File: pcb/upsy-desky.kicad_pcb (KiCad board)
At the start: 2 copper layers, 40.9 x 58 mm, 48 parts, among them J1 RJ45, J2 RJ45, J3 USB_C_ReceptacleUSB2.0, Q1 MMBT3904, Q2 MMBT3904, Q3 BSS138, Q4 BSS138, Q5 BSS138, Q6 BSS138, Q7 BSS138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

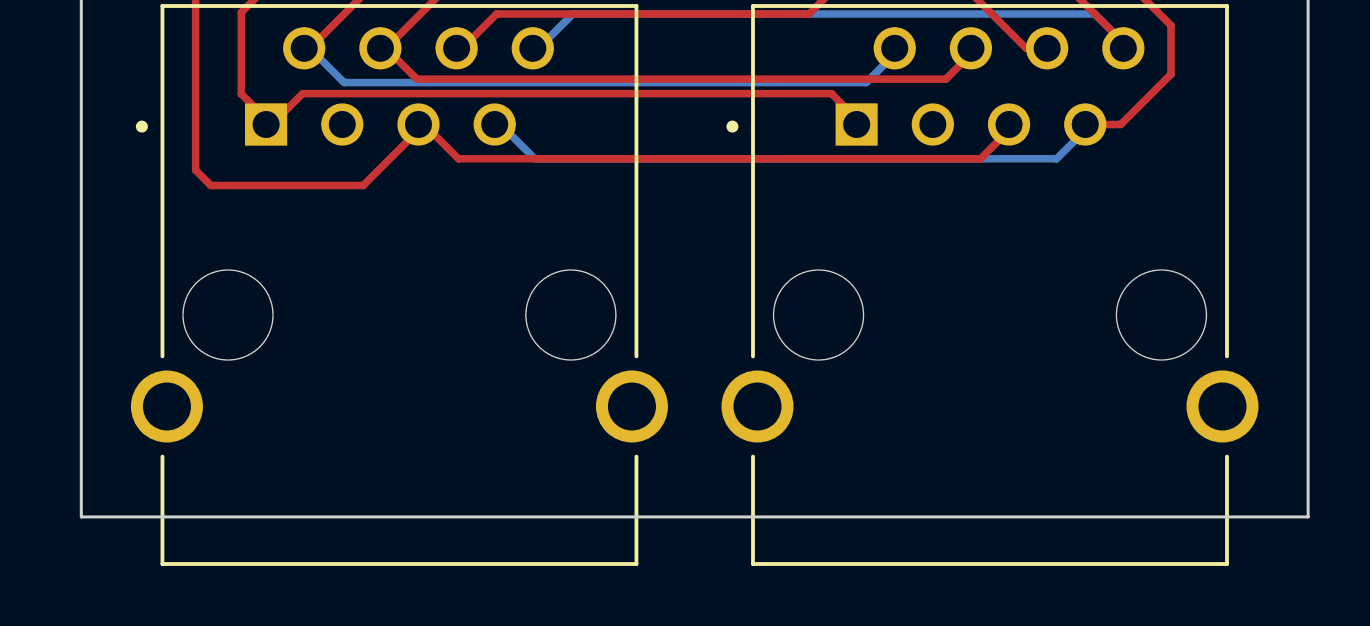
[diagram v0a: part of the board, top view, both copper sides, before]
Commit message: PCB: Change schematics to esp32 devkit
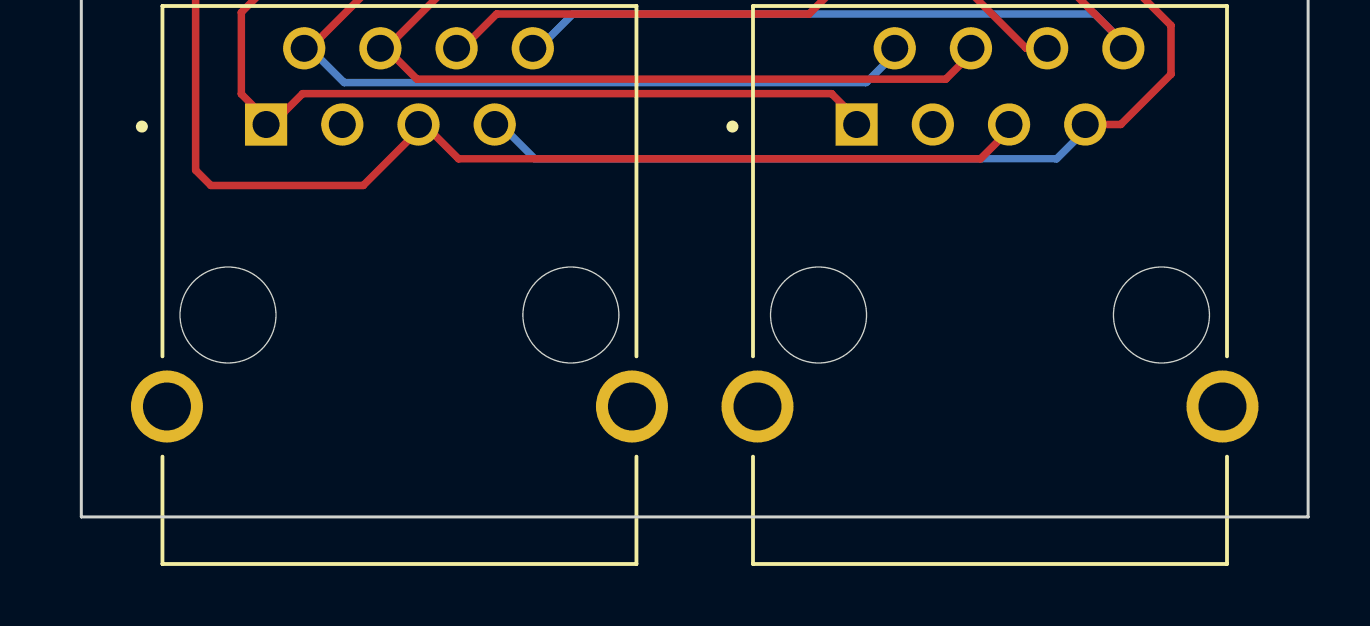
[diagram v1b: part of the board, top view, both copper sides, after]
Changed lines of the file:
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@@
       (effects (font (size 1.4 1.4) (thickness 0.15)))
     )
+    (fp_line (start 7.9 4.72) (end 7.9 8.3) (layer "F.SilkS") (width 0.127))
+    (fp_line (start -7.9 1.38) (end -7.9 -10.3) (layer "F.SilkS") (width 0.127))
+    (fp_line (start -7.9 -10.3) (end 7.9 -10.3) (layer "F.SilkS") (width 0.127))
+    (fp_line (start -7.9 8.3) (end -7.9 4.72) (layer "F.SilkS") (width 0.127))
     (fp_line (start 7.9 8.3) (end -7.9 8.3) (layer "F.SilkS") (width 0.127))
-    (fp_line (start 7.9 4.72) (end 7.9 8.3) (layer "F.SilkS") (width 0.127))
-    (fp_line (start -7.9 8.3) (end -7.9 4.72) (layer "F.SilkS") (width 0.127))
-    (fp_line (start -7.9 1.38) (end -7.9 -10.3) (layer "F.SilkS") (width 0.127))
     (fp_line (start 7.9 -10.3) (end 7.9 1.38) (layer "F.SilkS") (width 0.127))
-    (fp_line (start -7.9 -10.3) (end 7.9 -10.3) (layer "F.SilkS") (width 0.127))
     (fp_circle (center -8.586 -6.281) (end -8.486 -6.281) (layer "F.SilkS") (width 0.2) (fill none))
+    (fp_line (start 9.35 -10.55) (end -9.35 -10.55) (layer "F.CrtYd") (width 0.05))
+    (fp_line (start -9.35 -10.55) (end -9.35 8.55) (layer "F.CrtYd") (width 0.05))
+    (fp_line (start -9.35 8.55) (end 9.35 8.55) (layer "F.CrtYd") (width 0.05))
     (fp_line (start 9.35 8.55) (end 9.35 -10.55) (layer "F.CrtYd") (width 0.05))
-    (fp_line (start -9.35 -10.55) (end -9.35 8.55) (layer "F.CrtYd") (width 0.05))
-    (fp_line (start 9.35 -10.55) (end -9.35 -10.55) (layer "F.CrtYd") (width 0.05))
-    (fp_line (start -9.35 8.55) (end 9.35 8.55) (layer "F.CrtYd") (width 0.05))
     (fp_line (start -7.9 8.3) (end -7.9 -10.3) (layer "F.Fab") (width 0.127))
+    (fp_line (start -7.9 -10.3) (end 7.9 -10.3) (layer "F.Fab") (width 0.127))
     (fp_line (start 7.9 8.3) (end -7.9 8.3) (layer "F.Fab") (width 0.127))
-    (fp_line (start -7.9 -10.3) (end 7.9 -10.3) (layer "F.Fab") (width 0.127))
     (fp_line (start 7.9 -10.3) (end 7.9 8.3) (layer "F.Fab") (width 0.127))
     (fp_circle (center -8.586 -6.281) (end -8.486 -6.281) (layer "F.Fab") (width 0.2) (fill none))
-    (pad "" np_thru_hole circle (at -5.715 0) (size 3 3) (drill 3) (layers F&B.Cu *.Mask))
-    (pad "" np_thru_hole circle (at 5.715 0) (size 3 3) (drill 3) (layers F&B.Cu *.Mask))
+    (pad "" np_thru_hole circle (at -5.715 0) (size 3.2 3.2) (drill 3.2) (layers *.Cu *.Mask))
+    (pad "" np_thru_hole circle (at 5.715 0) (size 3.2 3.2) (drill 3.2) (layers *.Cu *.Mask))
     (pad "1" thru_hole rect (at -4.445 -6.35) (size 1.408 1.408) (drill 0.9) (layers *.Cu *.Mask)
       (net 16 "/DESK_1") (pinfunction "1") (pintype "passive"))
@@
       (net 1 "GND") (pinfunction "SHIELD__1") (pintype "passive"))
     (model "/Users/tj/Projects/deskcontroller/footprints/A-2004-2-4-LPS-N-R.step"
-      (offset (xyz 0 -8.3 6.8))
+      (offset (xyz 0 -8.3 6.6))
       (scale (xyz 1 1 1))
       (rotate (xyz -90 0 0))
@@
     )
     (fp_line (start -7.9 1.38) (end -7.9 -10.3) (layer "F.SilkS") (width 0.127))
-    (fp_line (start -7.9 8.3) (end -7.9 4.72) (layer "F.SilkS") (width 0.127))
+    (fp_line (start 7.9 4.72) (end 7.9 8.3) (layer "F.SilkS") (width 0.127))
+    (fp_line (start 7.9 8.3) (end -7.9 8.3) (layer "F.SilkS") (width 0.127))
     (fp_line (start 7.9 -10.3) (end 7.9 1.38) (layer "F.SilkS") (width 0.127))
     (fp_line (start -7.9 -10.3) (end 7.9 -10.3) (layer "F.SilkS") (width 0.127))
-    (fp_line (start 7.9 8.3) (end -7.9 8.3) (layer "F.SilkS") (width 0.127))
-    (fp_line (start 7.9 4.72) (end 7.9 8.3) (layer "F.SilkS") (width 0.127))
+    (fp_line (start -7.9 8.3) (end -7.9 4.72) (layer "F.SilkS") (width 0.127))
     (fp_circle (center -8.586 -6.281) (end -8.486 -6.281) (layer "F.SilkS") (width 0.2) (fill none))
     (fp_line (start 9.35 -10.55) (end -9.35 -10.55) (layer "F.CrtYd") (width 0.05))
@@
     (fp_line (start -9.35 8.55) (end 9.35 8.55) (layer "F.CrtYd") (width 0.05))
     (fp_line (start 9.35 8.55) (end 9.35 -10.55) (layer "F.CrtYd") (width 0.05))
+    (fp_line (start -7.9 -10.3) (end 7.9 -10.3) (layer "F.Fab") (width 0.127))
     (fp_line (start 7.9 8.3) (end -7.9 8.3) (layer "F.Fab") (width 0.127))
+    (fp_line (start 7.9 -10.3) (end 7.9 8.3) (layer "F.Fab") (width 0.127))
     (fp_line (start -7.9 8.3) (end -7.9 -10.3) (layer "F.Fab") (width 0.127))
-    (fp_line (start -7.9 -10.3) (end 7.9 -10.3) (layer "F.Fab") (width 0.127))
-    (fp_line (start 7.9 -10.3) (end 7.9 8.3) (layer "F.Fab") (width 0.127))
     (fp_circle (center -8.586 -6.281) (end -8.486 -6.281) (layer "F.Fab") (width 0.2) (fill none))
-    (pad "" np_thru_hole circle (at 5.715 0) (size 3 3) (drill 3) (layers F&B.Cu *.Mask))
-    (pad "" np_thru_hole circle (at -5.715 0) (size 3 3) (drill 3) (layers F&B.Cu *.Mask))
+    (pad "" np_thru_hole circle (at -5.715 0) (size 3.2 3.2) (drill 3.2) (layers *.Cu *.Mask))
+    (pad "" np_thru_hole circle (at 5.715 0) (size 3.2 3.2) (drill 3.2) (layers *.Cu *.Mask))
     (pad "1" thru_hole rect (at -4.445 -6.35) (size 1.408 1.408) (drill 0.9) (layers *.Cu *.Mask)
       (net 16 "/DESK_1") (pinfunction "1") (pintype "passive"))
@@
       (net 1 "GND") (pinfunction "SHIELD__1") (pintype "passive"))
     (model "/Users/tj/Projects/deskcontroller/footprints/A-2004-2-4-LPS-N-R.step"
-      (offset (xyz 0 -8.3 6.8))
+      (offset (xyz 0 -8.3 6.6))
       (scale (xyz 1 1 1))
       (rotate (xyz -90 0 0))
